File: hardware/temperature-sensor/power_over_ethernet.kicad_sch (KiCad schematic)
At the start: 1 part

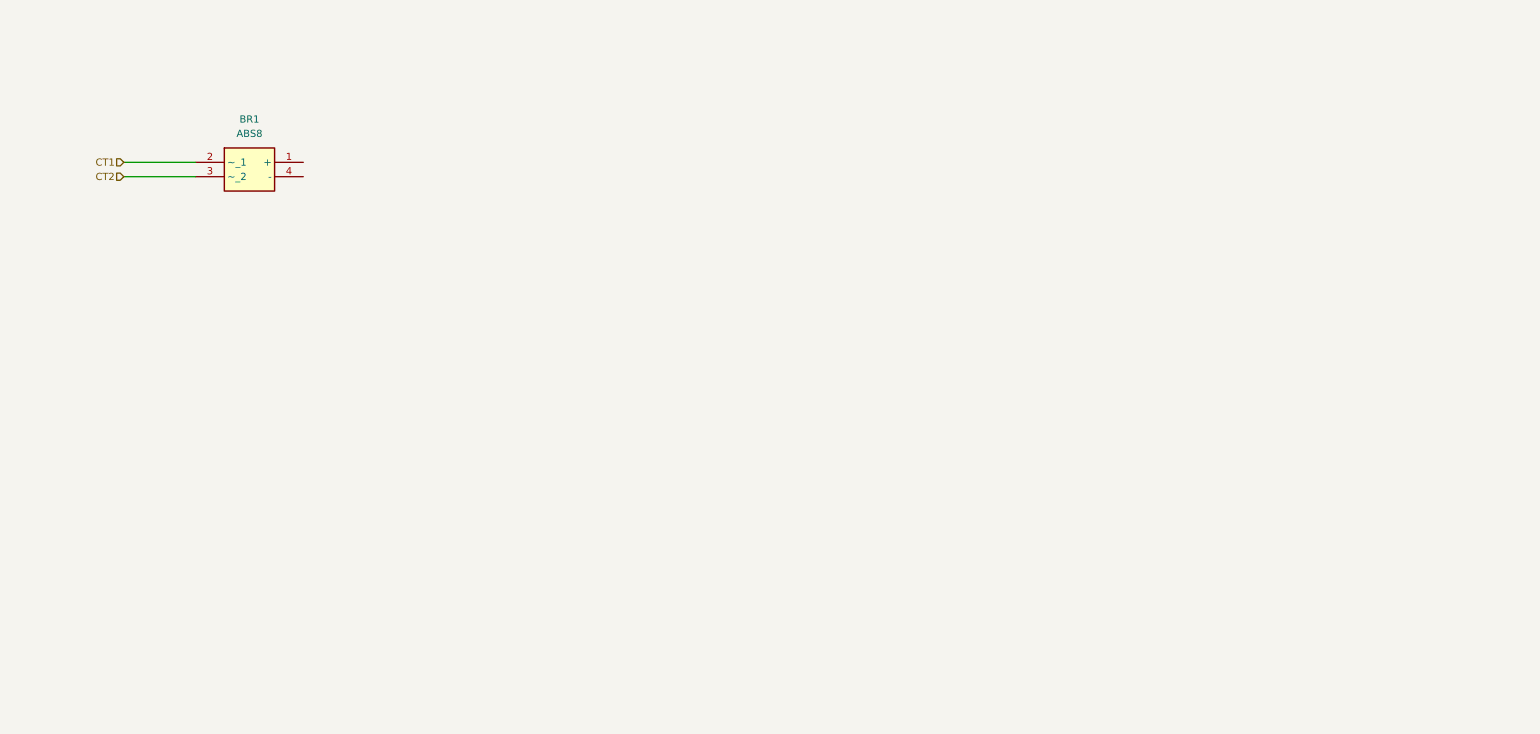
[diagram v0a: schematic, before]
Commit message: work on temperature sensor
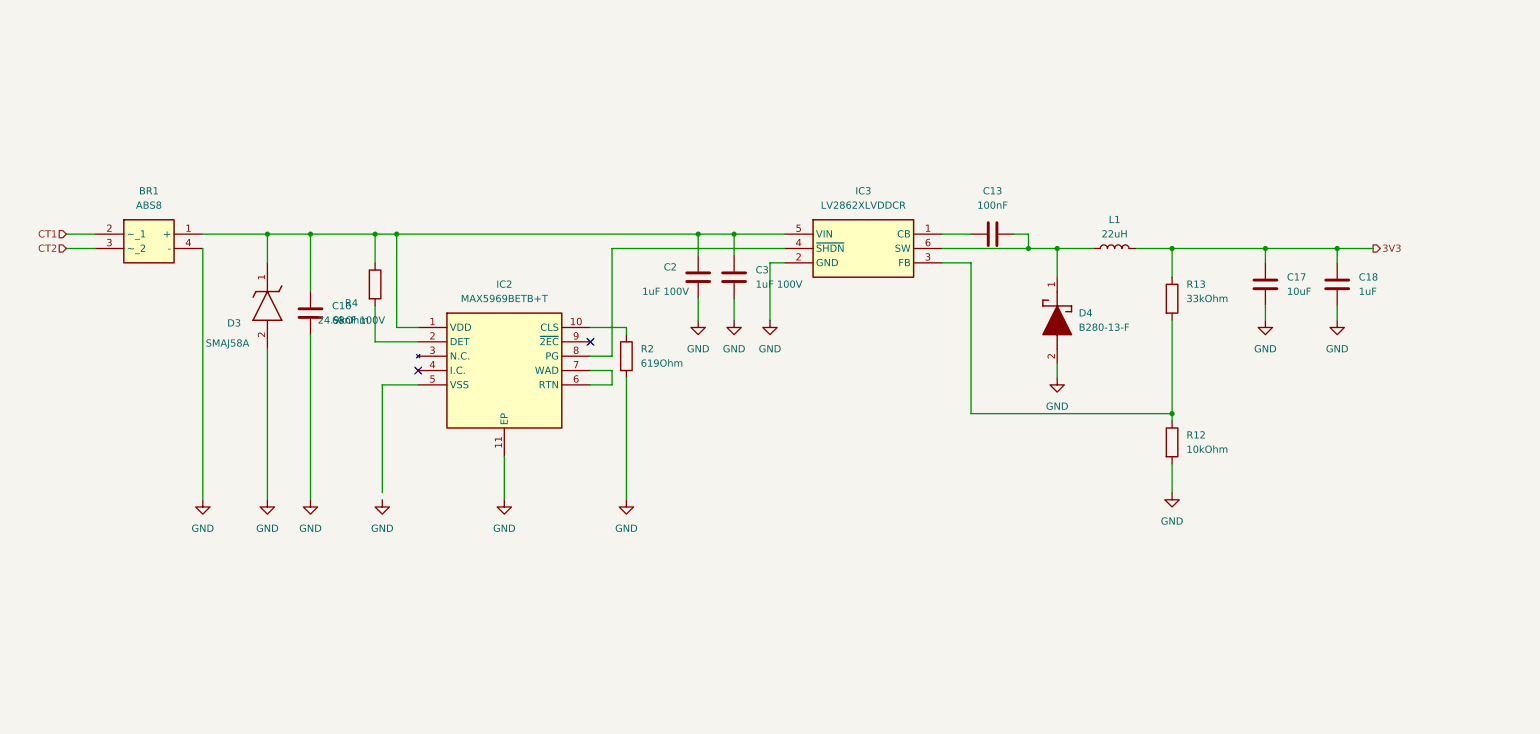
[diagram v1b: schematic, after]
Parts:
- added C13: 100nF, benediktibk:C_0603_1608Metric_Pad1.08x0.95mm_HandSolder, symbol benediktibk:C_100nF_SMD_0603_50V
- added C16: 68nF 100V, benediktibk:C_0603_1608Metric_Pad1.08x0.95mm_HandSolder, symbol benediktibk:C_68nF_SMD_0603_100V_10%
- added C17: 10uF, benediktibk:C_1210_3225Metric_Pad1.33x2.70mm_HandSolder, symbol benediktibk:C_10uF_SMD_1210_50V_20%
- added C18: 1uF, benediktibk:C_0603_1608Metric_Pad1.08x0.95mm_HandSolder, symbol benediktibk:C_1uF_SMD_0603_50V_10%
- added C2, C3: 1uF 100V, benediktibk:C_0603_1608Metric_Pad1.08x0.95mm_HandSolder, symbol benediktibk:C_1uF_SMD_0603_100V_10%
- added D3: SMAJ58A, benediktibk:DIOM5026X229N, symbol benediktibk:SMAJ58A
- added D4: B280-13-F, benediktibk:DIOM5336X250N, symbol benediktibk:B280-13-F
- added IC2: MAX5969BETB+T, benediktibk:SON50P300X300X80-11N, symbol benediktibk:MAX5969BETB+T
- added IC3: LV2862XLVDDCR, benediktibk:SOT95P280X110-6N, symbol benediktibk:LV2862XLVDDCR
- added L1: 22uH, benediktibk:L_Radial_D9.5mm_P5.00mm_Fastron_07HVP, symbol benediktibk:L_22uH_1_9A_9MHz_10%
- added R12: 10kOhm, benediktibk:R_0603_1608Metric_Pad0.98x0.95mm_HandSolder, symbol benediktibk:R_10kOhm_SMD_0603_100mW_1%
- added R13: 33kOhm, benediktibk:R_0603_1608Metric_Pad0.98x0.95mm_HandSolder, symbol benediktibk:R_33kOhm_SMD_0603_100mW_1%
- added R2: 619Ohm, benediktibk:R_0603_1608Metric_Pad0.98x0.95mm_HandSolder, symbol benediktibk:R_619Ohm_SMD_0603_100mW_1%
- added R4: 24.9kOhm, benediktibk:R_0603_1608Metric_Pad0.98x0.95mm_HandSolder, symbol benediktibk:R_24_9kOhm_SMD_0603_100mW_1%
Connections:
- net at BR1.1 (+): now also C16.1, C2.1, C3.1, D3.1 (K), IC2.1 (VDD), IC3.5 (VIN), R4.1
- net GND: now reaches BR1.4 (-)
- net GND: now also C16.2, C17.2, C18.2, C2.2, C3.2, D3.2 (A), D4.2 (A), IC2.11 (EP), IC3.2 (GND), R12.2, R2.2
- new net: IC3.3 (FB), R12.1, R13.2
- new net: IC2.2 (DET), R4.2
- new net: C13.1, D4.1 (K), IC3.6 (SW), L1.1
- new net: C13.2, IC3.1 (CB)
- new net: IC2.8 (PG), IC3.4 (~{SHDN})
- new net: IC2.10 (CLS), R2.1
- new net: IC2.6 (RTN), IC2.7 (WAD)
- new net 3V3: C17.1, C18.1, L1.2, R13.1
- no-connect marks 0 -> 2
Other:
- moved on the sheet: BR1

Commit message: work on temperature sensor
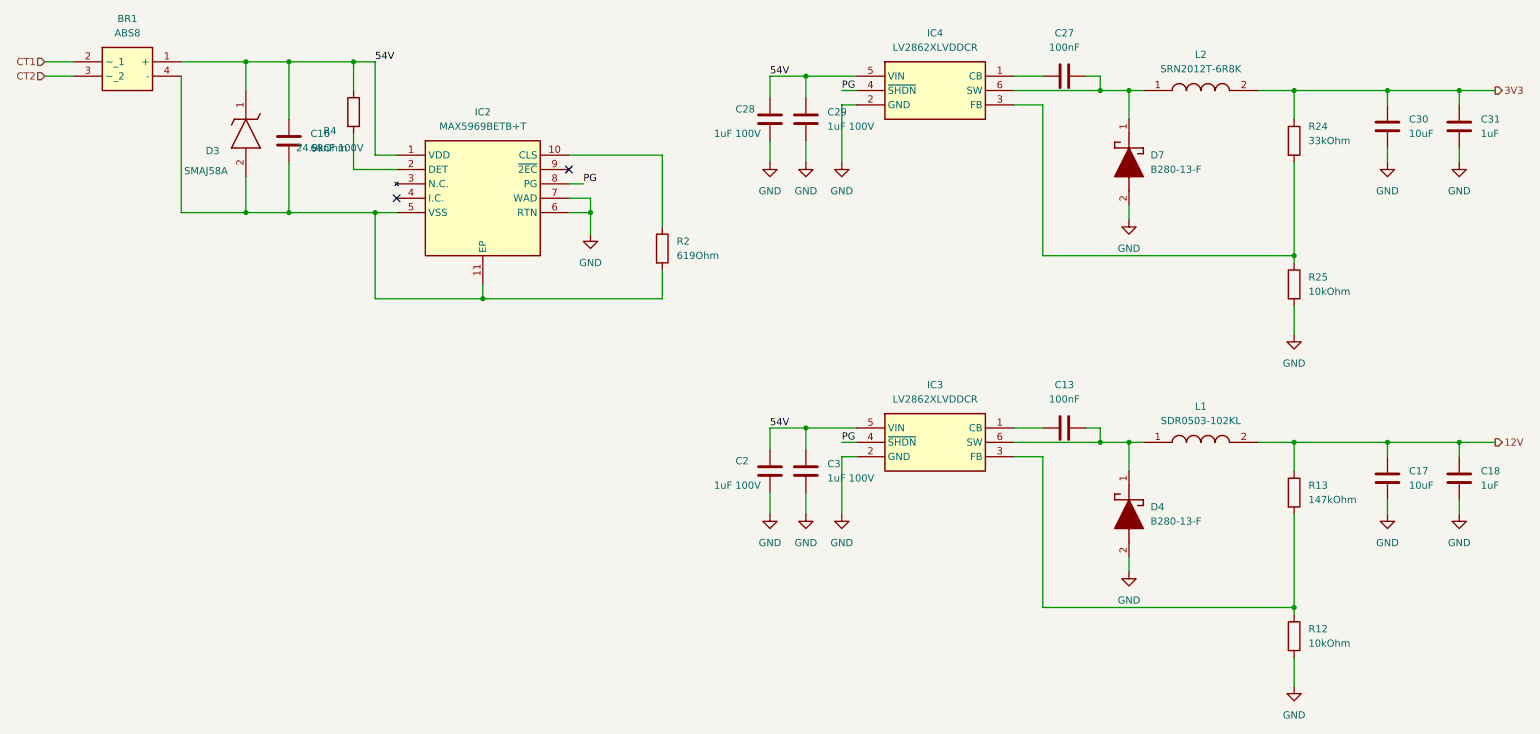
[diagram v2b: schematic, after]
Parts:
- removed L1: 22uH, benediktibk:L_Radial_D9.5mm_P5.00mm_Fastron_07HVP, symbol benediktibk:L_22uH_1_9A_9MHz_10%
- removed R13: 33kOhm, benediktibk:R_0603_1608Metric_Pad0.98x0.95mm_HandSolder, symbol benediktibk:R_33kOhm_SMD_0603_100mW_1%
- added C27: 100nF, benediktibk:C_0603_1608Metric_Pad1.08x0.95mm_HandSolder, symbol benediktibk:C_100nF_SMD_0603_50V
- added C28, C29: 1uF 100V, benediktibk:C_0603_1608Metric_Pad1.08x0.95mm_HandSolder, symbol benediktibk:C_1uF_SMD_0603_100V_10%
- added C30: 10uF, benediktibk:C_1210_3225Metric_Pad1.33x2.70mm_HandSolder, symbol benediktibk:C_10uF_SMD_1210_50V_20%
- added C31: 1uF, benediktibk:C_0603_1608Metric_Pad1.08x0.95mm_HandSolder, symbol benediktibk:C_1uF_SMD_0603_50V_10%
- added D7: B280-13-F, benediktibk:DIOM5336X250N, symbol benediktibk:B280-13-F
- added IC4: LV2862XLVDDCR, benediktibk:SOT95P280X110-6N, symbol benediktibk:LV2862XLVDDCR
- added L1: SDR0503-102KL, benediktibk:SDR0503102KL, symbol benediktibk:SDR0503-102KL
- added L2: SRN2012T-6R8K, benediktibk:INDPM2012X120N, symbol benediktibk:SRN2012T-6R8K
- added R13: 147kOhm, benediktibk:R_0603_1608Metric_Pad0.98x0.95mm_HandSolder, symbol benediktibk:R_147kOhm_SMD_0603_100mW_1%
- added R24: 33kOhm, benediktibk:R_0603_1608Metric_Pad0.98x0.95mm_HandSolder, symbol benediktibk:R_33kOhm_SMD_0603_100mW_1%
- added R25: 10kOhm, benediktibk:R_0603_1608Metric_Pad0.98x0.95mm_HandSolder, symbol benediktibk:R_10kOhm_SMD_0603_100mW_1%
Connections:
- net 3V3: now also C30.1, C31.1, L2.2, R24.1; no longer C17.1, C18.1
- net GND: now also IC2.6 (RTN), IC2.7 (WAD), C28.2, C29.2, C30.2, C31.2, D7.2 (A), IC4.2 (GND), R25.2; no longer BR1.4 (-), C16.2, D3.2 (A), IC2.11 (EP), R2.2
- net 54V: now reaches BR1.1 (+), C16.1, C2.1, C3.1, D3.1 (K), IC2.1 (VDD), IC3.5 (VIN), R4.1
- net 54V: now also C28.1, C29.1, IC4.5 (VIN)
- net at IC3.3 (FB), R12.1: now also R13.2
- net at C13.1, D4.1 (K), IC3.6 (SW): now also L1.1
- net PG: now reaches IC2.8 (PG), IC3.4 (~{SHDN})
- net PG: now also IC4.4 (~{SHDN})
- net at IC2.5 (VSS): now also BR1.4 (-), C16.2, D3.2 (A), IC2.11 (EP), R2.2
- new net: C27.1, D7.1 (K), IC4.6 (SW), L2.1
- new net: C27.2, IC4.1 (CB)
- new net: IC4.3 (FB), R24.2, R25.1
- new net 12V: C17.1, C18.1, L1.2, R13.1
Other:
- moved on the sheet: BR1, C13, C16, C17, C18, C2, C3, D3, D4, IC2, IC3, R12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

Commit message: update symbols from library
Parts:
- R2: Mouser Part Number 652-CR0603FX-1002ELF -> 603-RT0603FRE07619RL
- R24: Mouser Part Number 303-CQ03SAF3302T5E -> 594-MCT06030C3302FP5
- R4: Mouser Part Number 303-0603SAF2492T5E -> 594-MCT06030C2492FP5
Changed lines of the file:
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@@
 			)
 		)
-		(property "Mouser Part Number" "303-0603SAF2492T5E"
+		(property "Mouser Part Number" "594-MCT06030C2492FP5"
 			(at 57.15 30.48 0)
 			(effects
@@
 			)
 		)
-		(property "Mouser Part Number" "652-CR0603FX-1002ELF"
+		(property "Mouser Part Number" "603-RT0603FRE07619RL"
 			(at 111.76 54.61 0)
 			(effects
@@
 			)
 		)
-		(property "Mouser Part Number" "303-CQ03SAF3302T5E"
+		(property "Mouser Part Number" "594-MCT06030C3302FP5"
 			(at 243.84 39.3699 0)
 			(effects
